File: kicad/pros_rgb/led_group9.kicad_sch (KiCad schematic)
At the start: 8 parts

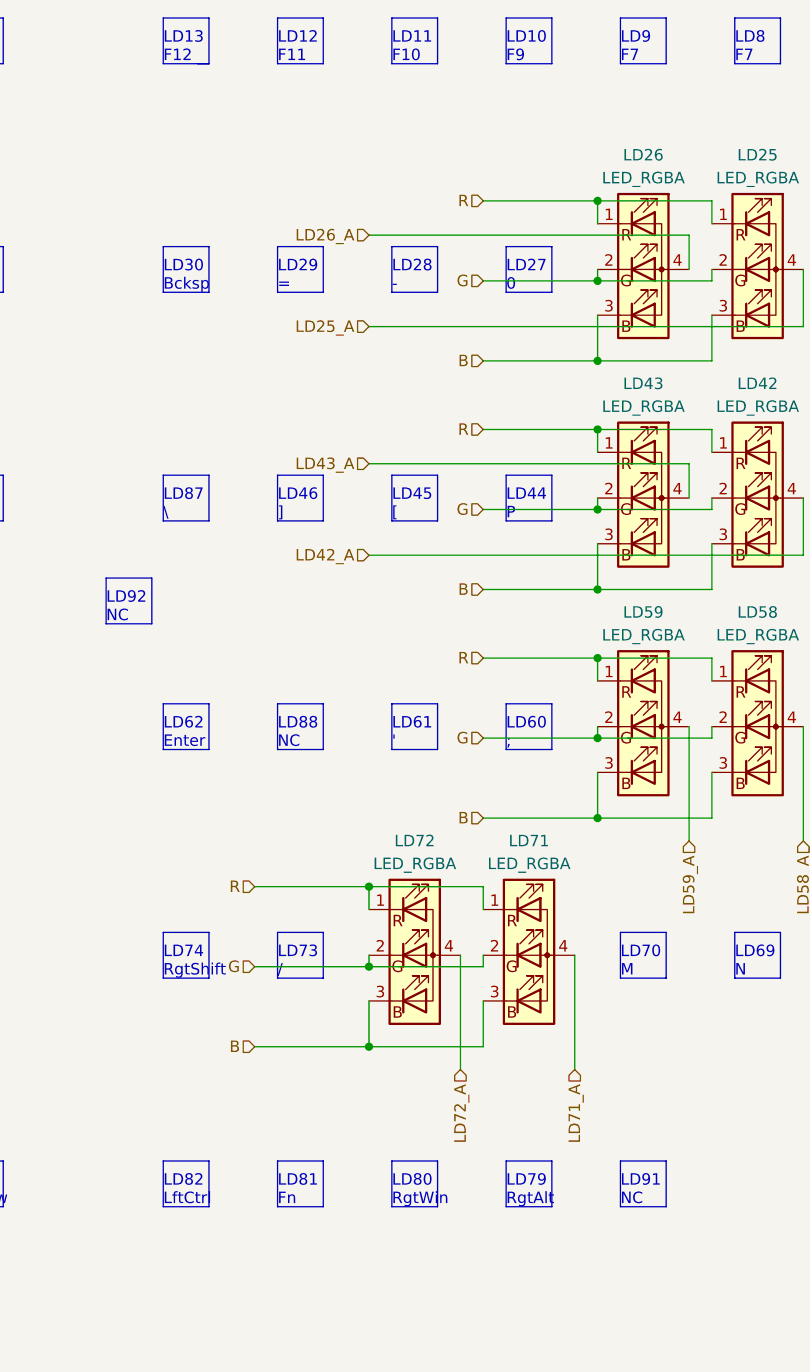
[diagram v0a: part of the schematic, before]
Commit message: kicad/pros_rgb: fix typos
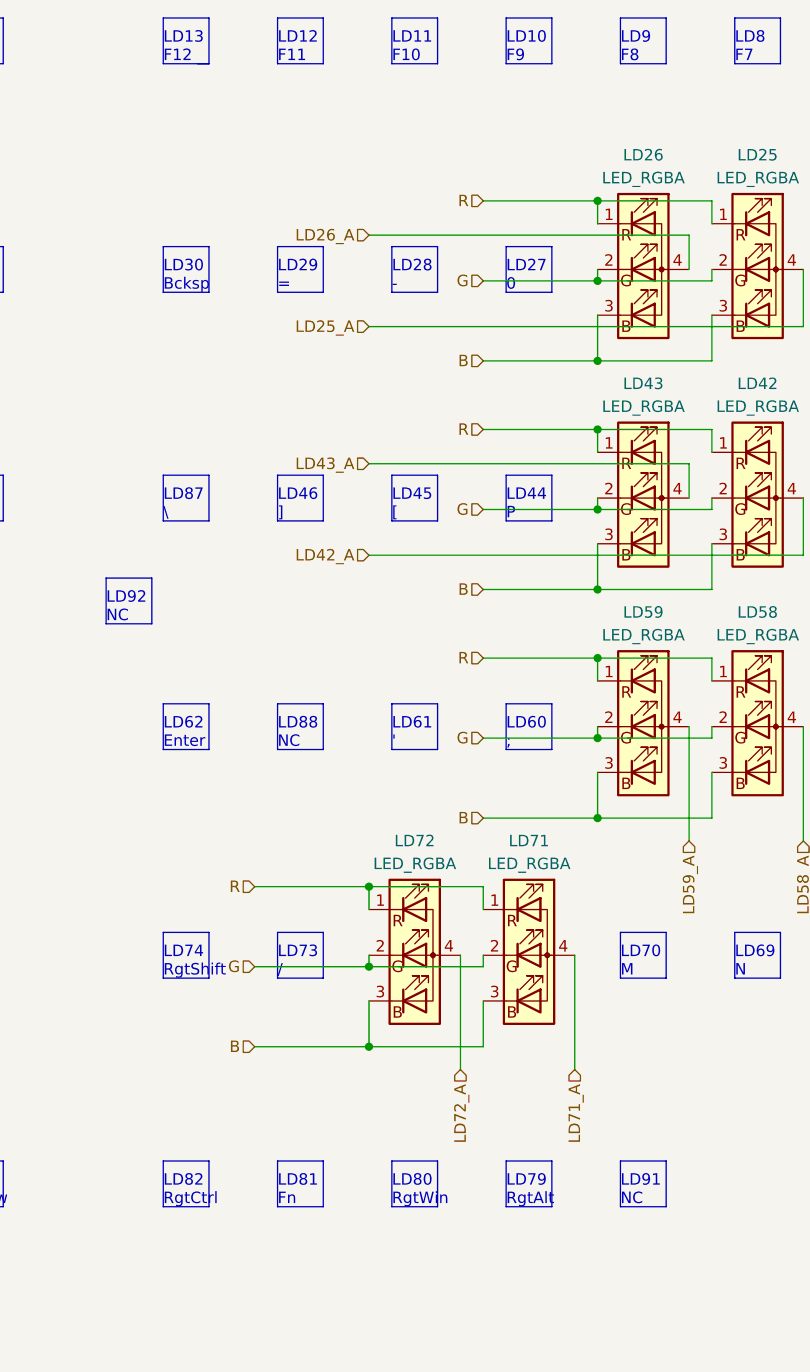
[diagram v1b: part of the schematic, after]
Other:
- note added: "LD82 RgtCtrl"
- note added: "LD9 F8"
- note removed: "LD82 LftCtrl"
- note removed: "LD9 F7"
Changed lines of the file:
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@@
     (effects (font (size 1.27 1.27)) (justify left bottom))
   )
-  (text "LD82\nLftCtrl" (at 106.68 156.21 0)
+  (text "LD82\nRgtCtrl" (at 106.68 156.21 0)
     (effects (font (size 1.27 1.27)) (justify left bottom))
   )
-  (text "LD9\nF7" (at 157.48 29.21 0)
+  (text "LD9\nF8" (at 157.48 29.21 0)
     (effects (font (size 1.27 1.27)) (justify left bottom))
   )

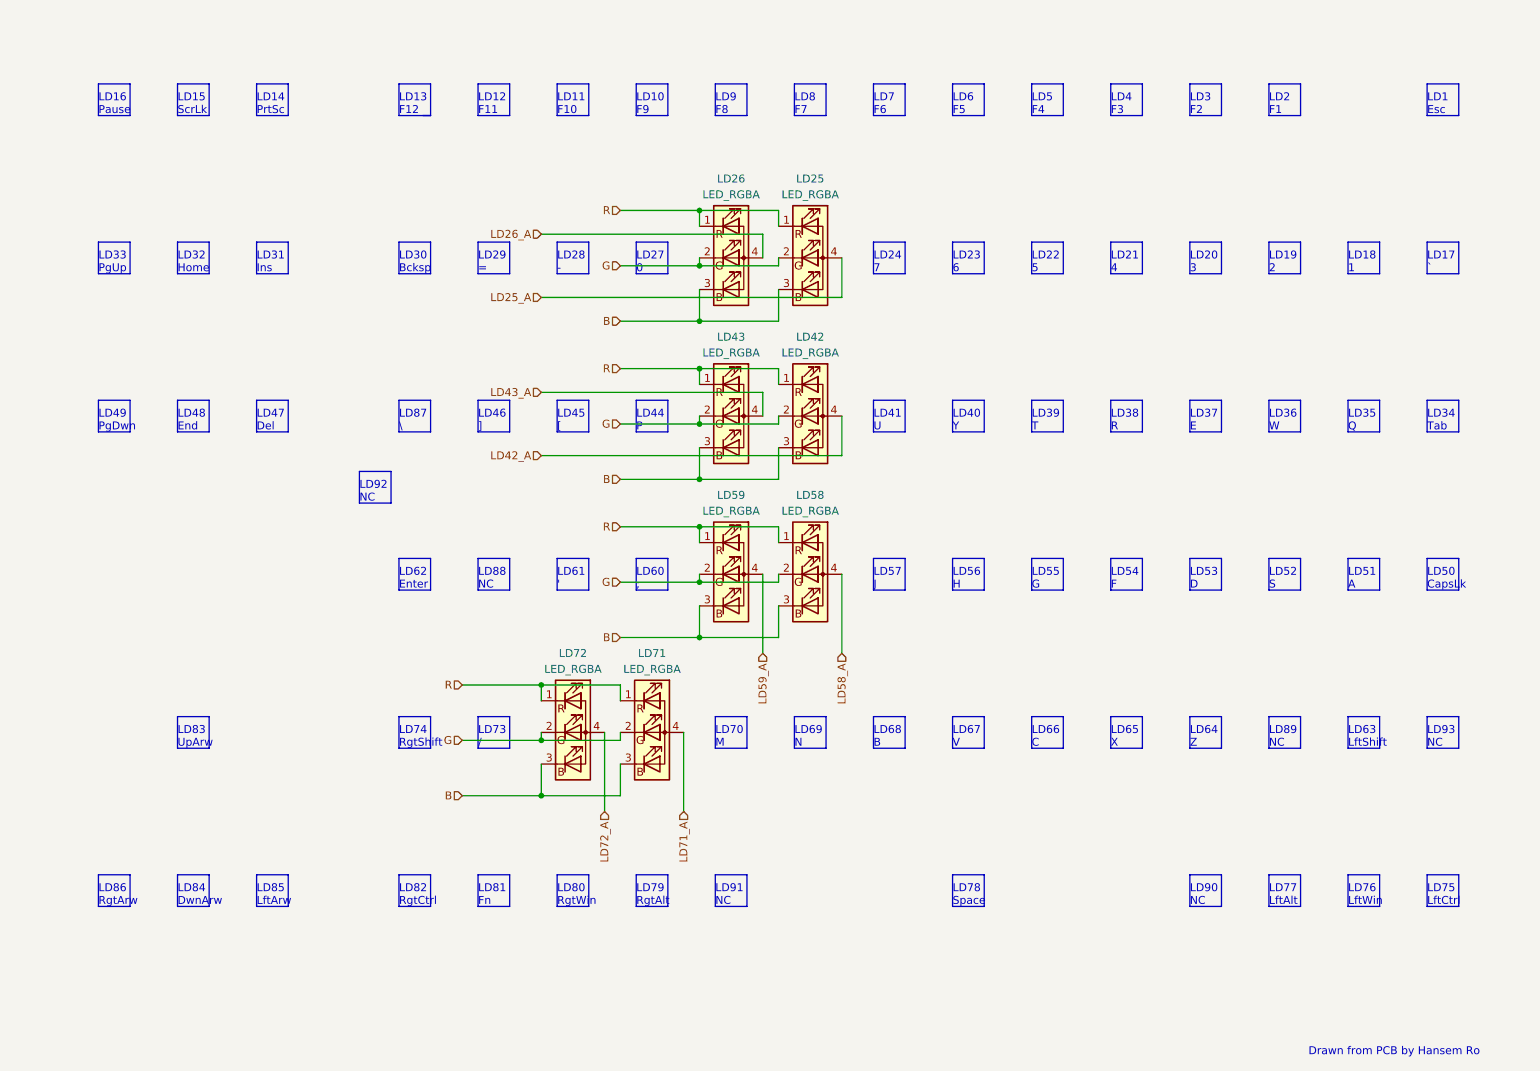
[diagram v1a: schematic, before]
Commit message: kicad/pros_rgb: order led groups by channel number
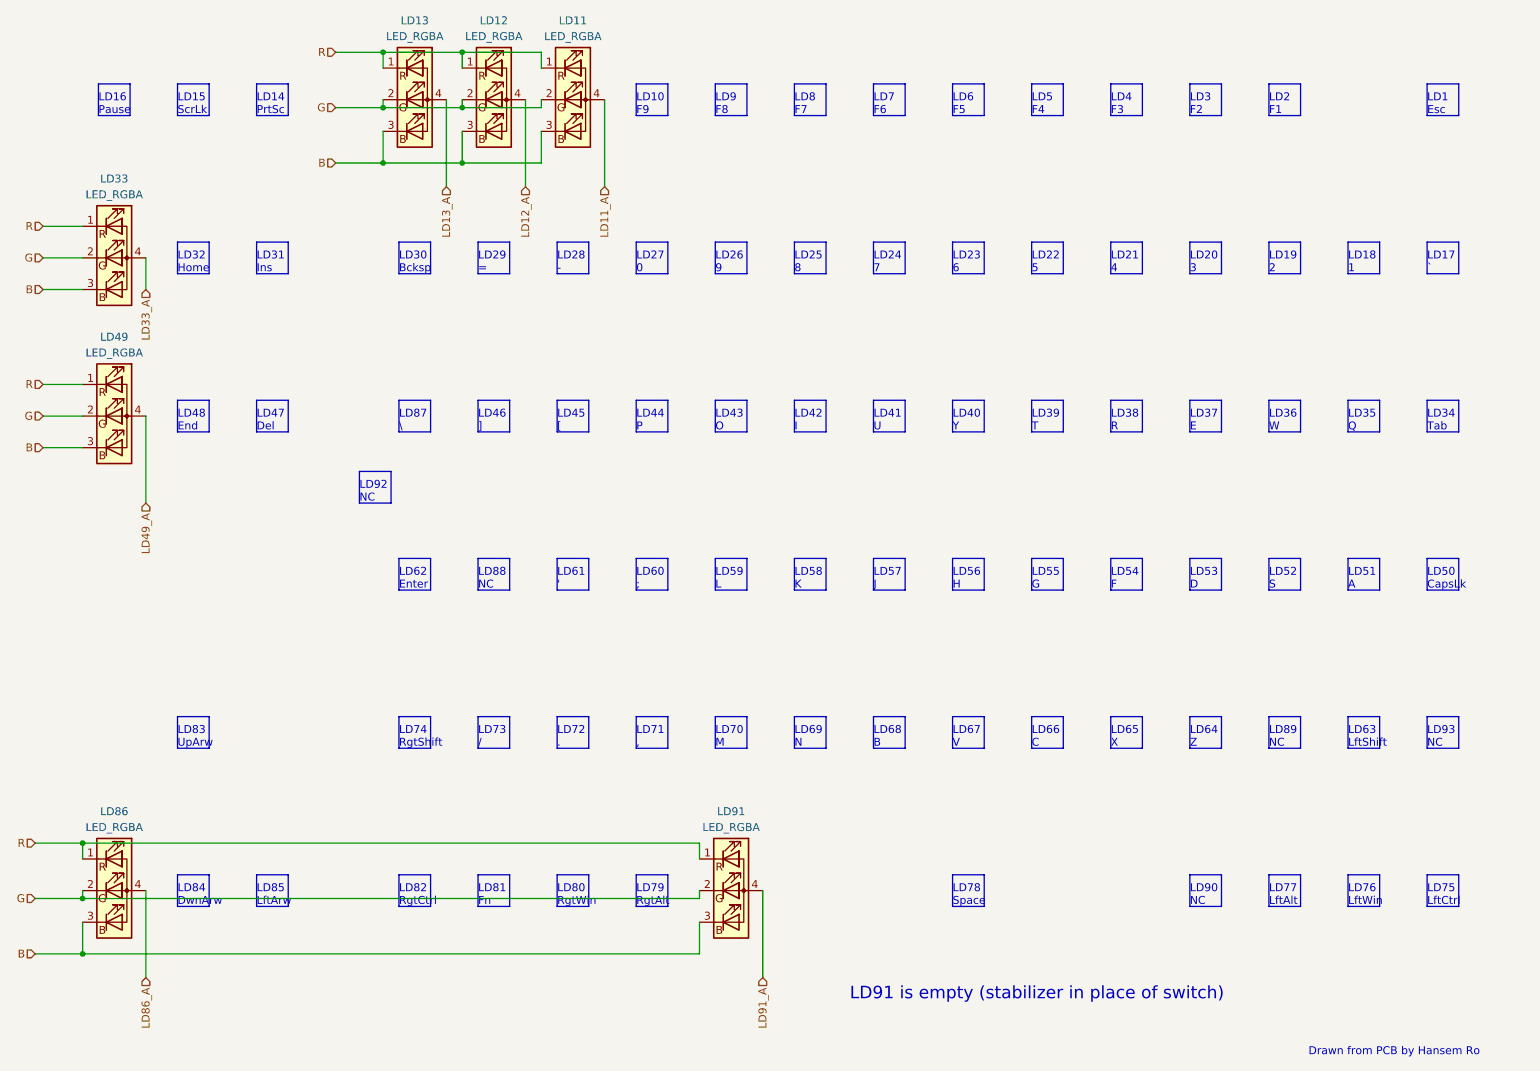
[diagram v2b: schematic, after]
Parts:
- removed LD25, LD26, LD42, LD43, LD58, LD59, LD71, LD72: LED_RGBA, symbol Device:LED_RGBA
- added LD11, LD12, LD13, LD33, LD49, LD86, LD91: LED_RGBA, symbol Device:LED_RGBA
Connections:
- net B: now also LD11.3 (BK), LD12.3 (BK), LD13.3 (BK), LD33.3 (BK), LD49.3 (BK), LD86.3 (BK), LD91.3 (BK)
- net G: now also LD11.2 (GK), LD12.2 (GK), LD13.2 (GK), LD33.2 (GK), LD49.2 (GK), LD86.2 (GK), LD91.2 (GK)
- net R: now also LD11.1 (RK), LD12.1 (RK), LD13.1 (RK), LD33.1 (RK), LD49.1 (RK), LD86.1 (RK), LD91.1 (RK)
- new net LD11_A: LD11.4 (A)
- new net LD12_A: LD12.4 (A)
- new net LD13_A: LD13.4 (A)
- new net LD33_A: LD33.4 (A)
- new net LD49_A: LD49.4 (A)
- new net LD86_A: LD86.4 (A)
- new net LD91_A: LD91.4 (A)
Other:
- note added: "LD25 8"
- note added: "LD26 9"
- note added: "LD42 I"
- note added: "LD43 O"
- note added: "LD58 K"
- note added: "LD59 L"
- note added: "LD71 ,"
- note added: "LD72 ."
- note added: "LD91 is empty (stabilizer in place of switch)"
- note removed: "LD11 F10"
- note removed: "LD12 F11"
- note removed: "LD13 F12"
- note removed: "LD33 PgUp"
- note removed: "LD49 PgDwn"
- note removed: "LD86 RgtArw"
- note removed: "LD91 NC"
